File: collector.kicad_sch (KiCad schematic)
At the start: 1 part, among them U11 74LS32

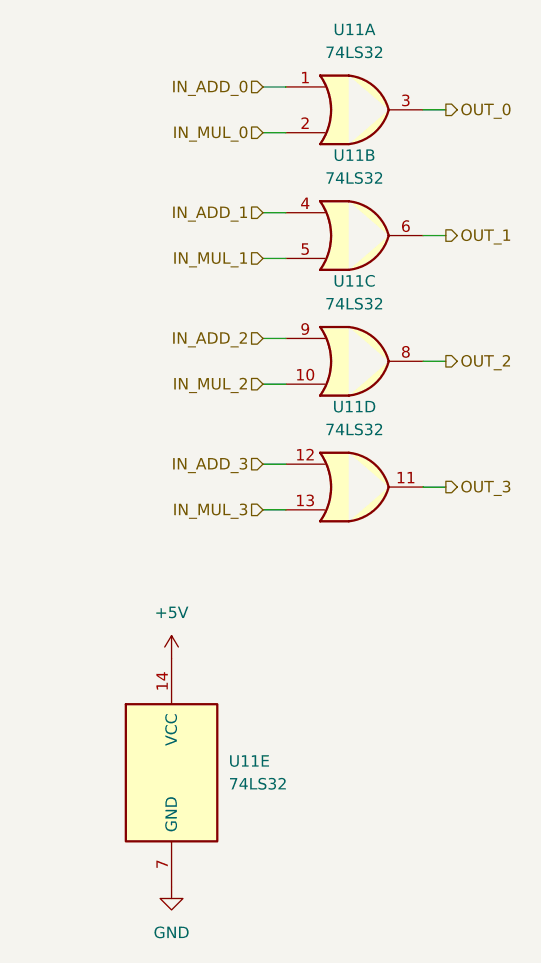
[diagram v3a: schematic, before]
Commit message: feat: footprints on gates
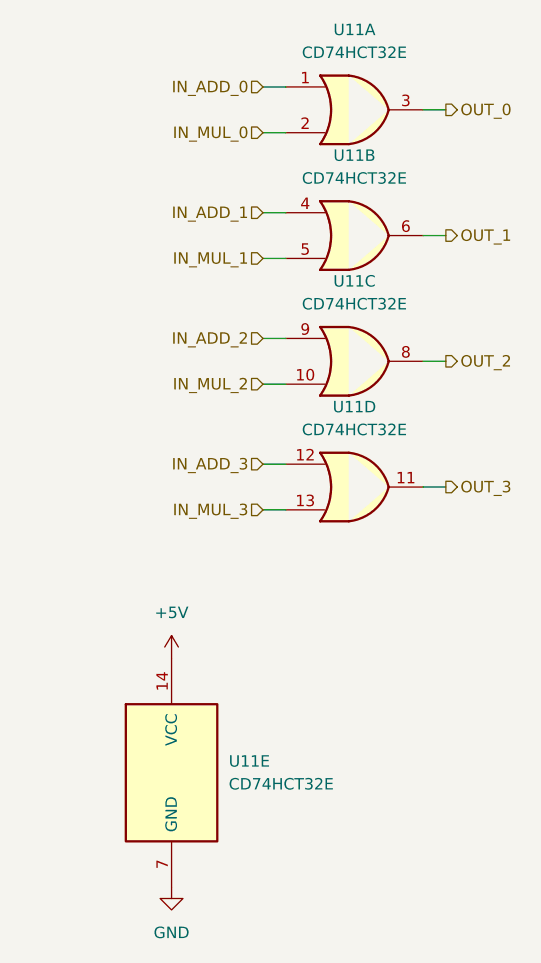
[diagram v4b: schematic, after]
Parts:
- U11: value 74LS32 -> CD74HCT32E; footprint (none) -> Package_DIP:DIP-14_W7.62mm_LongPads
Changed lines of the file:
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@@
 			)
 		)
-		(property "Value" "74LS32"
+		(property "Value" "CD74HCT32E"
 			(at 91.44 88.9 0)
 			(show_name no)
@@
 			)
 		)
-		(property "Footprint" ""
+		(property "Footprint" "Package_DIP:DIP-14_W7.62mm_LongPads"
 			(at 91.44 95.25 0)
 			(hide yes)
@@
 			)
 		)
-		(property "Datasheet" "http://www.ti.com/lit/gpn/sn74LS32"
+		(property "Datasheet" "https://www.ti.com/lit/ds/symlink/cd54hct32.pdf"
 			(at 91.44 95.25 0)
 			(hide yes)
@@
 			)
 		)
-		(property "Value" "74LS32"
+		(property "Value" "CD74HCT32E"
 			(at 77.47 128.2699 0)
 			(show_name no)
@@
 			)
 		)
-		(property "Footprint" ""
+		(property "Footprint" "Package_DIP:DIP-14_W7.62mm_LongPads"
 			(at 71.12 127 0)
 			(hide yes)
@@
 			)
 		)
-		(property "Datasheet" "http://www.ti.com/lit/gpn/sn74LS32"
+		(property "Datasheet" "https://www.ti.com/lit/ds/symlink/cd54hct32.pdf"
 			(at 71.12 127 0)
 			(hide yes)
@@
 			)
 		)
-		(property "Value" "74LS32"
+		(property "Value" "CD74HCT32E"
 			(at 91.44 74.93 0)
 			(show_name no)
@@
 			)
 		)
-		(property "Footprint" ""
+		(property "Footprint" "Package_DIP:DIP-14_W7.62mm_LongPads"
 			(at 91.44 81.28 0)
 			(hide yes)
@@
 			)
 		)
-		(property "Datasheet" "http://www.ti.com/lit/gpn/sn74LS32"
+		(property "Datasheet" "https://www.ti.com/lit/ds/symlink/cd54hct32.pdf"
 			(at 91.44 81.28 0)
 			(hide yes)
@@
 			)
 		)
-		(property "Value" "74LS32"
+		(property "Value" "CD74HCT32E"
 			(at 91.44 46.99 0)
 			(show_name no)
@@
 			)
 		)
-		(property "Footprint" ""
+		(property "Footprint" "Package_DIP:DIP-14_W7.62mm_LongPads"
 			(at 91.44 53.34 0)
 			(hide yes)
@@
 			)
 		)
-		(property "Datasheet" "http://www.ti.com/lit/gpn/sn74LS32"
+		(property "Datasheet" "https://www.ti.com/lit/ds/symlink/cd54hct32.pdf"
 			(at 91.44 53.34 0)
 			(hide yes)
@@
 			)
 		)
-		(property "Value" "74LS32"
+		(property "Value" "CD74HCT32E"
 			(at 91.44 60.96 0)
 			(show_name no)
@@
 			)
 		)
-		(property "Footprint" ""
+		(property "Footprint" "Package_DIP:DIP-14_W7.62mm_LongPads"
 			(at 91.44 67.31 0)
 			(hide yes)
@@
 			)
 		)
-		(property "Datasheet" "http://www.ti.com/lit/gpn/sn74LS32"
+		(property "Datasheet" "https://www.ti.com/lit/ds/symlink/cd54hct32.pdf"
 			(at 91.44 67.31 0)
 			(hide yes)

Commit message: feat: added capacitor with footprint
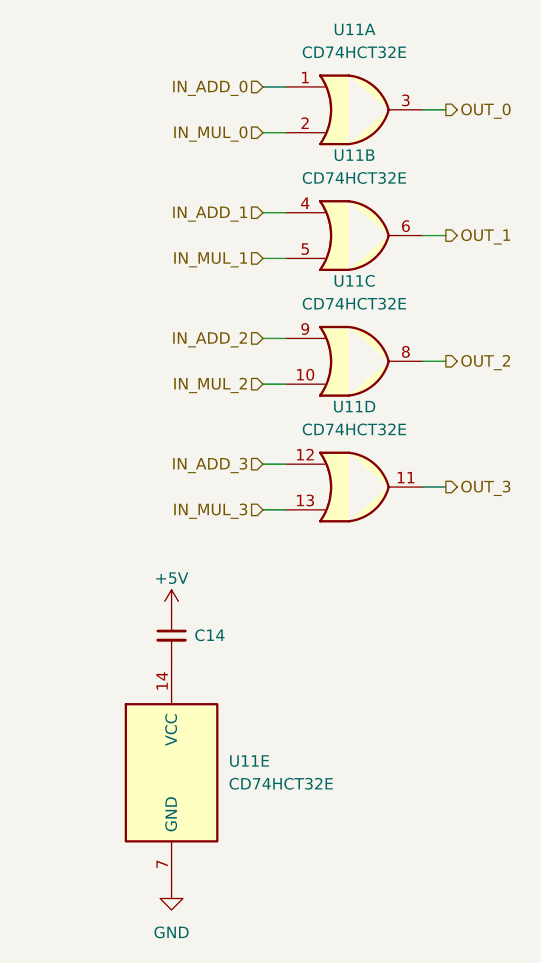
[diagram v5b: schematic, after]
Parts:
- added C14: C_Small, Capacitor_SMD:C_0603_1608Metric_Pad1.08x0.95mm_HandSolder, symbol Device:C_Small
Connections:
- net +5V: now also C14.1; no longer U11.14 (VCC)
- new net: C14.2, U11.14 (VCC)
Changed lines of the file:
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@@
+	)
+	(symbol
+		(lib_id "power:+5V")
+		(at 71.12 109.22 0)
+		(unit 1)
+		(body_style 1)
+		(exclude_from_sim no)
+		(in_bom yes)
+		(on_board yes)
+		(in_pos_files yes)
+		(dnp no)
+		(property "Reference" "#PWR041"
+			(at 71.12 113.03 0)
+			(hide yes)
+			(show_name no)
+			(do_not_autoplace no)
+			(effects
+				(font
+					(size 1.27 1.27)
+				)
+			)
+		)
+		(property "Value" "+5V"
+			(at 71.12 105.41 0)
+			(show_name no)
+			(do_not_autoplace no)
+			(effects
+				(font
+					(size 1.27 1.27)
+				)
+			)
+		)
+		(property "Footprint" ""
+			(at 71.12 109.22 0)
+			(hide yes)
+			(show_name no)
+			(do_not_autoplace no)
+			(effects
+				(font
+					(size 1.27 1.27)
+				)
+			)
+		)
+		(property "Datasheet" ""
+			(at 71.12 109.22 0)
+			(hide yes)
+			(show_name no)
+			(do_not_autoplace no)
+			(effects
+				(font
+					(size 1.27 1.27)
+				)
+			)
+		)
+		(property "Description" "Power symbol creates a global label with name \"+5V\""
+			(at 71.12 109.22 0)
+			(hide yes)
+			(show_name no)
+			(do_not_autoplace no)
+			(effects
+				(font
+					(size 1.27 1.27)
+				)
+			)
+		)
+		(pin "1"
+		)
+		(instances
+			(project "alu"
+				(path "/4987240f-8890-46b8-b8e9-0d60580cb205/5c1c7519-ef63-46db-b588-8e7d91f6be11"
+					(reference "#PWR041")
+					(unit 1)
+				)
+			)
+		)
 	)
 	(symbol
@@
 	)
 	(symbol
+		(lib_id "Device:C_Small")
+		(at 71.12 111.76 0)
+		(unit 1)
+		(body_style 1)
+		(exclude_from_sim no)
+		(in_bom yes)
+		(on_board yes)
+		(in_pos_files yes)
+		(dnp no)
+		(fields_autoplaced yes)
+		(property "Reference" "C14"
+			(at 73.66 111.7662 0)
+			(show_name no)
+			(do_not_autoplace no)
+			(effects
+				(font
+					(size 1.27 1.27)
+				)
+				(justify left)
+			)
+		)
+		(property "Value" "C_Small"
+			(at 73.66 113.0362 0)
+			(hide yes)
+			(show_name no)
+			(do_not_autoplace no)
+			(effects
+				(font
+					(size 1.27 1.27)
+				)
+				(justify left)
+			)
+		)
+		(property "Footprint" "Capacitor_SMD:C_0603_1608Metric_Pad1.08x0.95mm_HandSolder"
+			(at 71.12 111.76 0)
+			(hide yes)
+			(show_name no)
+			(do_not_autoplace no)
+			(effects
+				(font
+					(size 1.27 1.27)
+				)
+			)
+		)
+		(property "Datasheet" ""
+			(at 71.12 111.76 0)
+			(hide yes)
+			(show_name no)
+			(do_not_autoplace no)
+			(effects
+				(font
+					(size 1.27 1.27)
+				)
+			)
+		)
+		(property "Description" "Unpolarized capacitor, small symbol"
+			(at 71.12 111.76 0)
+			(hide yes)
+			(show_name no)
+			(do_not_autoplace no)
+			(effects
+				(font
+					(size 1.27 1.27)
+				)
+			)
+		)
+		(pin "2"
+		)
+		(pin "1"
+		)
+		(instances
+			(project "alu"
+				(path "/4987240f-8890-46b8-b8e9-0d60580cb205/5c1c7519-ef63-46db-b588-8e7d91f6be11"
+					(reference "C14")
+					(unit 1)
+				)
+			)
+		)
+	)
+	(symbol
 		(lib_id "74xx:74LS32")
 		(at 91.44 81.28 0)
@@
 					(unit 1)
 				)
-			)
-		)
-	)
-	(symbol
-		(lib_id "power:+5V")
-		(at 71.12 114.3 0)
-		(unit 1)
-		(body_style 1)
-		(exclude_from_sim no)
-		(in_bom yes)
-		(on_board yes)
-		(in_pos_files yes)
-		(dnp no)
-		(fields_autoplaced yes)
-		(property "Reference" "#PWR044"
-			(at 71.12 118.11 0)
-			(hide yes)
-			(show_name no)
-			(do_not_autoplace no)
-			(effects
-				(font
-					(size 1.27 1.27)
-				)
-			)
-		)
-		(property "Value" "+5V"
-			(at 71.12 109.22 0)
-			(show_name no)
-			(do_not_autoplace no)
-			(effects
-				(font
-					(size 1.27 1.27)
-				)
-			)
-		)
-		(property "Footprint" ""
-			(at 71.12 114.3 0)
-			(hide yes)
-			(show_name no)
-			(do_not_autoplace no)
-			(effects
-				(font
-					(size 1.27 1.27)
-				)
-			)
-		)
-		(property "Datasheet" ""
-			(at 71.12 114.3 0)
-			(hide yes)
-			(show_name no)
-			(do_not_autoplace no)
-			(effects
-				(font
-					(size 1.27 1.27)
-				)
-			)
-		)
-		(property "Description" "Power symbol creates a global label with name \"+5V\""
-			(at 71.12 114.3 0)
-			(hide yes)
-			(show_name no)
-			(do_not_autoplace no)
-			(effects
-				(font
-					(size 1.27 1.27)
-				)
-			)
-		)
-		(pin "1"
-		)
-		(instances
-			(project "alu"
-				(path "/4987240f-8890-46b8-b8e9-0d60580cb205/5c1c7519-ef63-46db-b588-8e7d91f6be11"
-					(reference "#PWR044")
-					(unit 1)
-				)

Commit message: fix: merge
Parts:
- renumbered U11 to U14
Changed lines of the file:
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@@
 		(in_pos_files yes)
 		(dnp no)
-		(property "Reference" "#PWR041"
+		(property "Reference" "#PWR?"
 			(at 71.12 113.03 0)
 			(hide yes)
@@
 			(project "alu"
 				(path "/4987240f-8890-46b8-b8e9-0d60580cb205/5c1c7519-ef63-46db-b588-8e7d91f6be11"
-					(reference "#PWR041")
+					(reference "#PWR?")
 					(unit 1)
 				)
@@
 		(dnp no)
 		(fields_autoplaced yes)
-		(property "Reference" "#PWR043"
+		(property "Reference" "#PWR?"
 			(at 71.12 146.05 0)
 			(hide yes)
@@
 			(project "alu"
 				(path "/4987240f-8890-46b8-b8e9-0d60580cb205/5c1c7519-ef63-46db-b588-8e7d91f6be11"
-					(reference "#PWR043")
+					(reference "#PWR?")
 					(unit 1)
 				)
@@
 		(dnp no)
 		(fields_autoplaced yes)
-		(property "Reference" "U11"
+		(property "Reference" "U14"
 			(at 91.44 86.36 0)
 			(show_name no)
@@
 			(project "alu"
 				(path "/4987240f-8890-46b8-b8e9-0d60580cb205/5c1c7519-ef63-46db-b588-8e7d91f6be11"
-					(reference "U11")
+					(reference "U14")
 					(unit 4)
 				)
@@
 		(dnp no)
 		(fields_autoplaced yes)
-		(property "Reference" "U11"
+		(property "Reference" "U14"
 			(at 77.47 125.7299 0)
 			(show_name no)
@@
 			(project "alu"
 				(path "/4987240f-8890-46b8-b8e9-0d60580cb205/5c1c7519-ef63-46db-b588-8e7d91f6be11"
-					(reference "U11")
+					(reference "U14")
 					(unit 5)
 				)
@@
 		(dnp no)
 		(fields_autoplaced yes)
-		(property "Reference" "U11"
+		(property "Reference" "U14"
 			(at 91.44 72.39 0)
 			(show_name no)
@@
 			(project "alu"
 				(path "/4987240f-8890-46b8-b8e9-0d60580cb205/5c1c7519-ef63-46db-b588-8e7d91f6be11"
-					(reference "U11")
+					(reference "U14")
 					(unit 3)
 				)
@@
 		(dnp no)
 		(fields_autoplaced yes)
-		(property "Reference" "U11"
+		(property "Reference" "U14"
 			(at 91.44 44.45 0)
 			(show_name no)
@@
 			(project "alu"
 				(path "/4987240f-8890-46b8-b8e9-0d60580cb205/5c1c7519-ef63-46db-b588-8e7d91f6be11"
-					(reference "U11")
+					(reference "U14")
 					(unit 1)
 				)
@@
 		(dnp no)
 		(fields_autoplaced yes)
-		(property "Reference" "U11"
+		(property "Reference" "U14"
 			(at 91.44 58.42 0)
 			(show_name no)
@@
 			(project "alu"
 				(path "/4987240f-8890-46b8-b8e9-0d60580cb205/5c1c7519-ef63-46db-b588-8e7d91f6be11"
-					(reference "U11")
+					(reference "U14")
 					(unit 2)
 				)

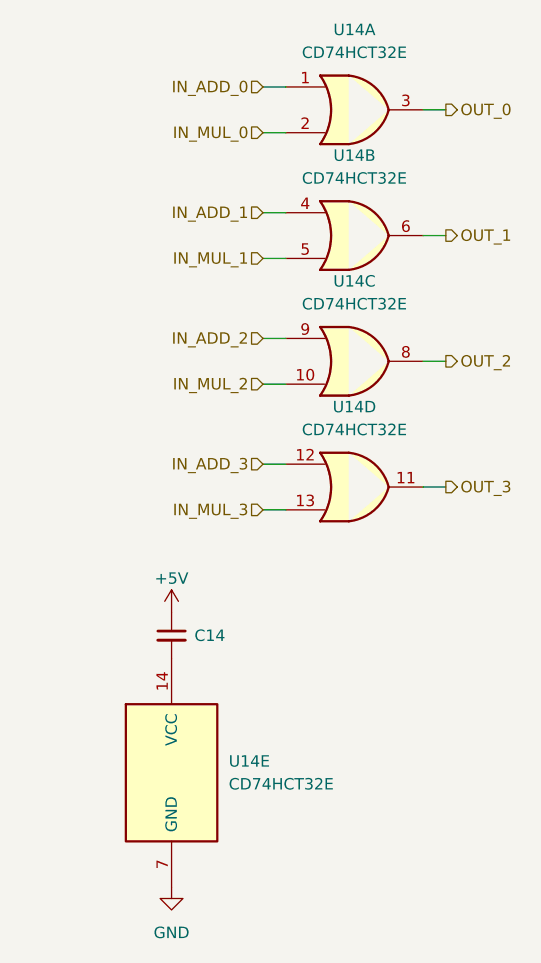
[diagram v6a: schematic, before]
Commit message: fix: capacitor collector/add
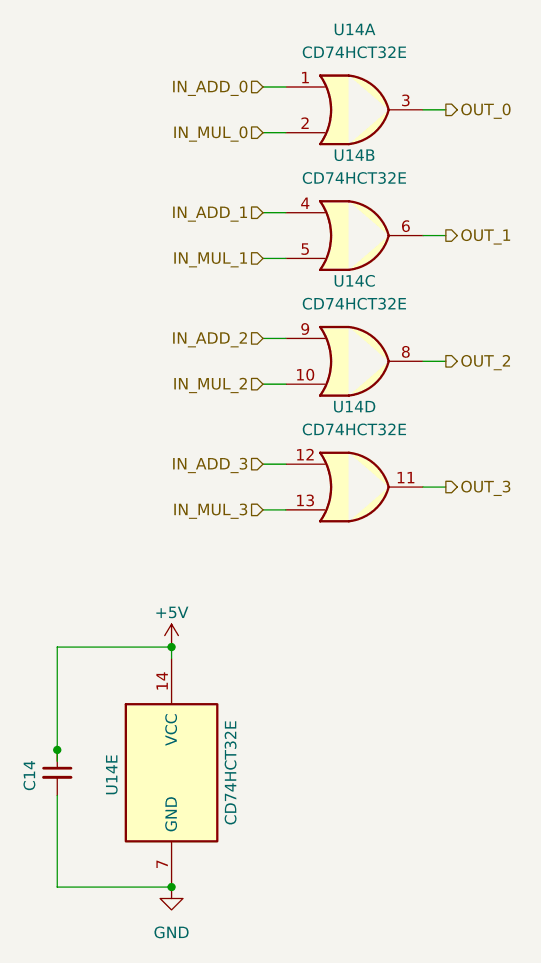
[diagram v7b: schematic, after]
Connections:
- net +5V: now also U14.14 (VCC)
- net GND: now also C14.2
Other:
- moved on the sheet: C14
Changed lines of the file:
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@@
 	(generator_version "10.0")
 	(paper "A4")
+	(junction
+		(at 58.42 124.46)
+		(diameter 0)
+		(color 0 0 0 0)
+	)
+	(junction
+		(at 71.12 139.7)
+		(diameter 0)
+		(color 0 0 0 0)
+	)
+	(junction
+		(at 71.12 113.03)
+		(diameter 0)
+		(color 0 0 0 0)
+	)
 	(wire
 		(pts
@@
 	(wire
 		(pts
+			(xy 58.42 124.46) (xy 58.42 113.03)
+		)
+		(stroke
+			(width 0)
+			(type default)
+		)
+	)
+	(wire
+		(pts
+			(xy 58.42 125.73) (xy 58.42 124.46)
+		)
+		(stroke
+			(width 0)
+			(type default)
+		)
+	)
+	(wire
+		(pts
+			(xy 58.42 113.03) (xy 71.12 113.03)
+		)
+		(stroke
+			(width 0)
+			(type default)
+		)
+	)
+	(wire
+		(pts
 			(xy 81.28 83.82) (xy 83.82 83.82)
 		)
@@
 	(wire
 		(pts
+			(xy 58.42 139.7) (xy 71.12 139.7)
+		)
+		(stroke
+			(width 0)
+			(type default)
+		)
+	)
+	(wire
+		(pts
 			(xy 81.28 78.74) (xy 83.82 78.74)
 		)
@@
 		(pts
 			(xy 81.28 92.71) (xy 83.82 92.71)
+		)
+		(stroke
+			(width 0)
+			(type default)
+		)
+	)
+	(wire
+		(pts
+			(xy 58.42 129.54) (xy 58.42 139.7)
+		)
+		(stroke
+			(width 0)
+			(type default)
+		)
+	)
+	(wire
+		(pts
+			(xy 71.12 113.03) (xy 71.12 114.3)
 		)
 		(stroke
@@
 	(symbol
 		(lib_id "power:+5V")
-		(at 71.12 109.22 0)
+		(at 71.12 113.03 0)
 		(unit 1)
 		(body_style 1)
@@
 		(in_pos_files yes)
 		(dnp no)
-		(property "Reference" "#PWR?"
+		(property "Reference" "#PWR047"
+			(at 71.12 116.84 0)
+			(hide yes)
+			(show_name no)
+			(do_not_autoplace no)
+			(effects
+				(font
+					(size 1.27 1.27)
+				)
+			)
+		)
+		(property "Value" "+5V"
+			(at 71.12 109.22 0)
+			(show_name no)
+			(do_not_autoplace no)
+			(effects
+				(font
+					(size 1.27 1.27)
+				)
+			)
+		)
+		(property "Footprint" ""
 			(at 71.12 113.03 0)
 			(hide yes)
@@
 			)
 		)
-		(property "Value" "+5V"
-			(at 71.12 105.41 0)
-			(show_name no)
-			(do_not_autoplace no)
-			(effects
-				(font
-					(size 1.27 1.27)
-				)
-			)
-		)
-		(property "Footprint" ""
-			(at 71.12 109.22 0)
-			(hide yes)
-			(show_name no)
-			(do_not_autoplace no)
-			(effects
-				(font
-					(size 1.27 1.27)
-				)
-			)
-		)
 		(property "Datasheet" ""
-			(at 71.12 109.22 0)
+			(at 71.12 113.03 0)
 			(hide yes)
 			(show_name no)
@@
 		)
 		(property "Description" "Power symbol creates a global label with name \"+5V\""
-			(at 71.12 109.22 0)
+			(at 71.12 113.03 0)
 			(hide yes)
 			(show_name no)
@@
 			(project "alu"
 				(path "/4987240f-8890-46b8-b8e9-0d60580cb205/5c1c7519-ef63-46db-b588-8e7d91f6be11"
-					(reference "#PWR?")
+					(reference "#PWR047")
 					(unit 1)
 				)
@@
 		(dnp no)
 		(fields_autoplaced yes)
-		(property "Reference" "#PWR?"
+		(property "Reference" "#PWR048"
 			(at 71.12 146.05 0)
 			(hide yes)
@@
 			(project "alu"
 				(path "/4987240f-8890-46b8-b8e9-0d60580cb205/5c1c7519-ef63-46db-b588-8e7d91f6be11"
-					(reference "#PWR?")
+					(reference "#PWR048")
 					(unit 1)
 				)
@@
 		(in_pos_files yes)
 		(dnp no)
-		(fields_autoplaced yes)
 		(property "Reference" "U14"
-			(at 77.47 125.7299 0)
+			(at 64.516 129.54 90)
 			(show_name no)
 			(do_not_autoplace no)
@@
 		)
 		(property "Value" "CD74HCT32E"
-			(at 77.47 128.2699 0)
+			(at 77.724 132.842 90)
 			(show_name no)
 			(do_not_autoplace no)
@@
 	(symbol
 		(lib_id "Device:C_Small")
-		(at 71.12 111.76 0)
+		(at 58.42 127 0)
 		(unit 1)
 		(body_style 1)
@@
 		(in_pos_files yes)
 		(dnp no)
-		(fields_autoplaced yes)
 		(property "Reference" "C14"
-			(at 73.66 111.7662 0)
+			(at 55.372 129.032 90)
 			(show_name no)
 			(do_not_autoplace no)
@@
 		)
 		(property "Value" "C_Small"
-			(at 73.66 113.0362 0)
+			(at 60.96 128.2762 0)
 			(hide yes)
 			(show_name no)
@@
 		)
 		(property "Footprint" "Capacitor_SMD:C_0603_1608Metric_Pad1.08x0.95mm_HandSolder"
-			(at 71.12 111.76 0)
+			(at 58.42 127 0)
 			(hide yes)
 			(show_name no)
@@
 		)
 		(property "Datasheet" ""
-			(at 71.12 111.76 0)
+			(at 58.42 127 0)
 			(hide yes)
 			(show_name no)
@@
 		)
 		(property "Description" "Unpolarized capacitor, small symbol"
-			(at 71.12 111.76 0)
-			(hide yes)
-			(show_name no)
+			(at 58.42 127 0)
+			(hide yes)
+			(show_name no)

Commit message: fix: 0 error 0 warning
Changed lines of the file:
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@@
 	(paper "A4")
-	(junction
-		(at 58.42 124.46)
-		(diameter 0)
-		(color 0 0 0 0)
-	)
 	(junction
 		(at 71.12 139.7)
@@
 		(pts
 			(xy 81.28 50.8) (xy 83.82 50.8)
-		)
-		(stroke
-			(width 0)
-			(type default)
-		)
-	)
-	(wire
-		(pts
-			(xy 58.42 124.46) (xy 58.42 113.03)
-		)
-		(stroke
-			(width 0)
-			(type default)
-		)
-	)
-	(wire
-		(pts
-			(xy 58.42 125.73) (xy 58.42 124.46)
 		)
 		(stroke
@@
 		)
 		(stroke
+			(width 0)
+			(type default)
+		)
+	)
+	(wire
+		(pts
+			(xy 58.42 113.03) (xy 58.42 124.46)
+		)
+		(stroke
